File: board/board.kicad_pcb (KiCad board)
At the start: 2 copper layers, 45 x 29 mm, 32 parts, among them J1 019_100BASE-T_with_CT, J2 LPJ4265BDNL, U2 MP8007, U3 POE30P-50L

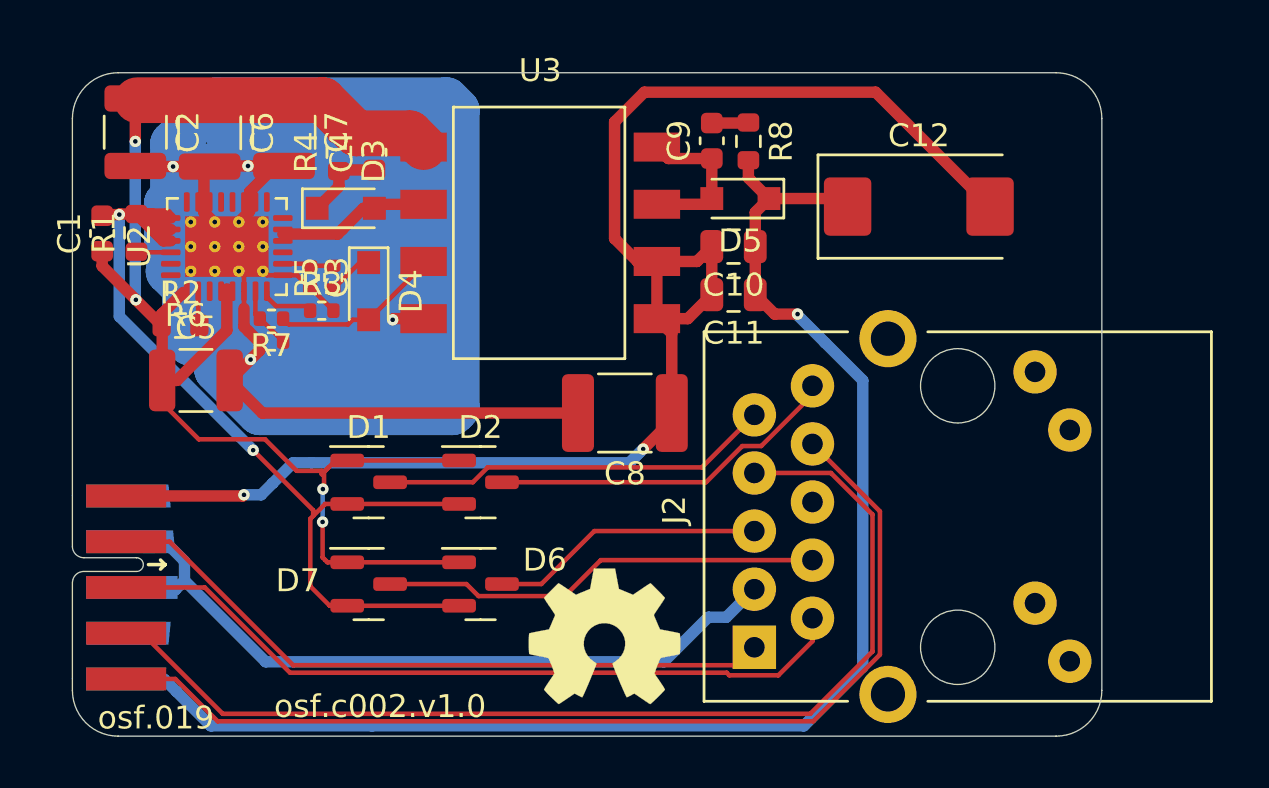
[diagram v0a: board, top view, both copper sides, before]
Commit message: cleaned up silkscreen
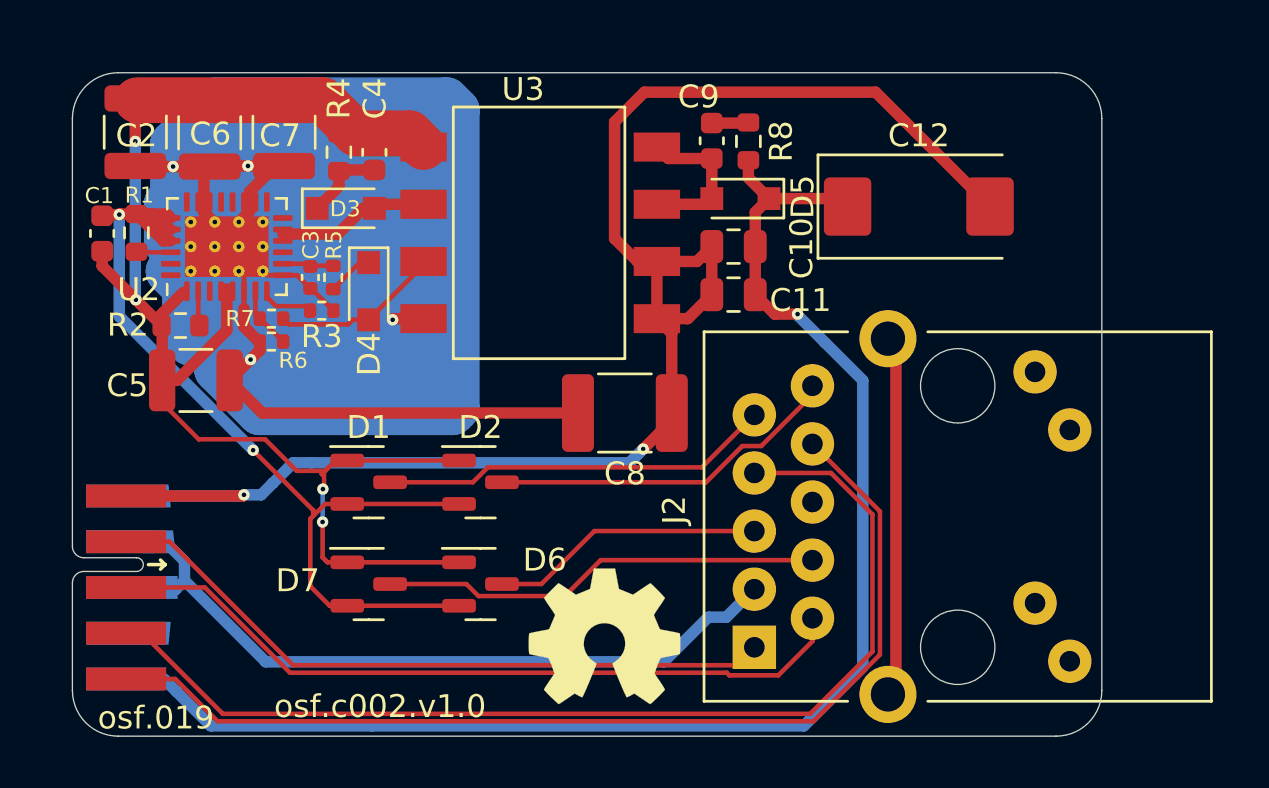
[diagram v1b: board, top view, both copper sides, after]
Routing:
- net /magjack/SH: track 0.00 -> 15.8 mm
- net GND: track 66.4 -> 71.5 mm
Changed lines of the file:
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@@
     (property "Voltage" "100V")
     (attr smd)
-    (fp_text reference "C2" (at 0 -2.3 90) (layer "F.SilkS")
+    (fp_text reference "C2" (at 0.15 -0.05 180) (layer "F.SilkS")
       (effects (font (size 1 1) (thickness 0.15)))
     )
@@
     (property "Sheetname" "Controller")
     (attr smd)
-    (fp_text reference "D5" (at 0 -1.85) (layer "F.SilkS")
+    (fp_text reference "D5" (at -2.725 0.075 90) (layer "F.SilkS")
       (effects (font (size 1 1) (thickness 0.15)))
     )
@@
     (property "Voltage" "100V")
     (attr smd)
-    (fp_text reference "C4" (at 0 -1.43 90) (layer "F.SilkS")
+    (fp_text reference "C4" (at 2.35 0.025 90) (layer "F.SilkS")
       (effects (font (size 1 1) (thickness 0.15)))
     )
@@
     (property "Sheetname" "Controller")
     (attr smd)
-    (fp_text reference "R1" (at 0 -1.43 90) (layer "F.SilkS")
-      (effects (font (size 1 1) (thickness 0.15)))
+    (fp_text reference "R1" (at 1.65 0.125 180) (layer "F.SilkS")
+      (effects (font (size 0.7 0.7) (thickness 0.15)))
     )
     (fp_text value "41.2R" (at 0 1.43 90) (layer "F.Fab")
@@
     (property "Sheetname" "Controller")
     (attr smd)
-    (fp_text reference "D4" (at 0 -1.85 90) (layer "F.SilkS")
+    (fp_text reference "D4" (at 2.75 -0.025 90) (layer "F.SilkS")
       (effects (font (size 1 1) (thickness 0.15)))
     )
@@
     (property "Sheetname" "Controller")
     (attr smd)
-    (fp_text reference "D3" (at 1.22 -2.07 90) (layer "F.SilkS")
-      (effects (font (size 1 1) (thickness 0.15)))
+    (fp_text reference "D3" (at -0.025 0.025 180) (layer "F.SilkS")
+      (effects (font (size 0.7 0.7) (thickness 0.15)))
     )
     (fp_text value "BAV21WS-HE3-18" (at 0.1 1.9) (layer "F.Fab")
@@
     (property "Sheetname" "Controller")
     (attr smd)
-    (fp_text reference "C3" (at 0 -1.16 90) (layer "F.SilkS")
-      (effects (font (size 1 1) (thickness 0.15)))
+    (fp_text reference "C3" (at -1.425 -0.025 90) (layer "F.SilkS")
+      (effects (font (size 0.7 0.7) (thickness 0.15)))
     )
     (fp_text value "100nF" (at 0 1.16 90) (layer "F.Fab")
@@
     (property "Voltage" "100V")
     (attr smd)
-    (fp_text reference "C5" (at 0 -2.3) (layer "F.SilkS")
+    (fp_text reference "C5" (at -3 0.225) (layer "F.SilkS")
       (effects (font (size 1 1) (thickness 0.15)))
     )
@@
     (property "Sheetname" "Controller")
     (attr through_hole)
-    (fp_text reference "U3" (at 0 -7.1) (layer "F.SilkS")
+    (fp_text reference "U3" (at -0.75 -6.275) (layer "F.SilkS")
       (effects (font (size 1 1) (thickness 0.15)))
     )
@@
     (property "Sheetname" "Controller")
     (attr smd)
-    (fp_text reference "R7" (at 0 -1.17) (layer "F.SilkS")
-      (effects (font (size 1 1) (thickness 0.15)))
+    (fp_text reference "R7" (at 1.375 0) (layer "F.SilkS")
+      (effects (font (size 0.7 0.7) (thickness 0.15)))
     )
     (fp_text value "100k" (at 0 1.17) (layer "F.Fab")
@@
     (property "Voltage" "100V")
     (attr smd)
-    (fp_text reference "C9" (at 0 -1.43 90) (layer "F.SilkS")
+    (fp_text reference "C9" (at 1.925 -0.575 180) (layer "F.SilkS")
       (effects (font (size 1 1) (thickness 0.15)))
     )
@@
     (property "Voltage" "6.3V")
     (attr smd)
-    (fp_text reference "C11" (at 0 -1.68) (layer "F.SilkS")
+    (fp_text reference "C11" (at -2.925 -0.25) (layer "F.SilkS")
       (effects (font (size 1 1) (thickness 0.15)))
     )
@@
     (property "Voltage" "100V")
     (attr smd)
-    (fp_text reference "C7" (at 0 -2.3 90) (layer "F.SilkS")
+    (fp_text reference "C7" (at 0.15 0.175 180) (layer "F.SilkS")
       (effects (font (size 1 1) (thickness 0.15)))
     )
@@
     (property "Sheetname" "Controller")
     (attr smd)
-    (fp_text reference "R6" (at -3.75 -1.145) (layer "F.SilkS")
-      (effects (font (size 1 1) (thickness 0.15)))
+    (fp_text reference "R6" (at 0.95 0.825) (layer "F.SilkS")
+      (effects (font (size 0.7 0.7) (thickness 0.15)))
     )
     (fp_text value "20k" (at 0 1.17) (layer "F.Fab")
@@
     (property "Sheetname" "Controller")
     (attr smd)
-    (fp_text reference "U2" (at 0 -3.82 90) (layer "F.SilkS")
+    (fp_text reference "U2" (at -1.875 -3.85 180) (layer "F.SilkS")
       (effects (font (size 1 1) (thickness 0.15)))
     )
@@
     (property "Voltage" "6.3V")
     (attr smd)
-    (fp_text reference "C10" (at 0 -1.68) (layer "F.SilkS")
+    (fp_text reference "C10" (at -2.975 -0.075 90) (layer "F.SilkS")
       (effects (font (size 1 1) (thickness 0.15)))
     )
@@
     (property "Sheetname" "Controller")
     (attr smd)
-    (fp_text reference "R2" (at 0 -1.43) (layer "F.SilkS")
+    (fp_text reference "R2" (at -2.3 -0.025) (layer "F.SilkS")
       (effects (font (size 1 1) (thickness 0.15)))
     )
@@
     (property "Voltage" "100V")
     (attr smd)
-    (fp_text reference "C6" (at 0 -2.3 90) (layer "F.SilkS")
+    (fp_text reference "C6" (at 0.05 -0.025 180) (layer "F.SilkS")
       (effects (font (size 1 1) (thickness 0.15)))
     )
@@
     (property "Sheetname" "Controller")
     (attr smd)
-    (fp_text reference "R5" (at 0 -1.17 90) (layer "F.SilkS")
-      (effects (font (size 1 1) (thickness 0.15)))
+    (fp_text reference "R5" (at 1.425 0.025 90) (layer "F.SilkS")
+      (effects (font (size 0.7 0.7) (thickness 0.15)))
     )
     (fp_text value "5k" (at 0 1.17 90) (layer "F.Fab")
@@
     (property "Sheetname" "Controller")
     (attr smd)
-    (fp_text reference "R4" (at 0 -1.43 90) (layer "F.SilkS")
+    (fp_text reference "R4" (at 2.35 0 90) (layer "F.SilkS")
       (effects (font (size 1 1) (thickness 0.15)))
     )
@@
     (property "Sheetname" "Controller")
     (attr smd)
-    (fp_text reference "C1" (at 0 -1.43 90) (layer "F.SilkS")
-      (effects (font (size 1 1) (thickness 0.15)))
+    (fp_text reference "C1" (at 1.65 -0.125 180) (layer "F.SilkS")
+      (effects (font (size 0.7 0.7) (thickness 0.15)))
     )
     (fp_text value "100n" (at 0 1.43 90) (layer "F.Fab")
@@
     (property "Sheetname" "Controller")
     (attr smd)
-    (fp_text reference "R3" (at 0 -1.17) (layer "F.SilkS")
+    (fp_text reference "R3" (at 0 1.125) (layer "F.SilkS")
       (effects (font (size 1 1) (thickness 0.15)))
     )
@@
   (segment (start 155.35 77.25) (end 154.75 76.65) (width 2) (layer "F.Cu") (net 1))
   (segment (start 150.95 75.2) (end 142.825 75.2) (width 2) (layer "F.Cu") (net 1))
-  (segment (start 146.025 75.125) (end 146 75.15) (width 0.5) (layer "F.Cu") (net 1))
   (segment (start 149.8 91.4) (end 150.9 91.4) (width 0.2) (layer "F.Cu") (net 1))
   (segment (start 156.9025 95.4) (end 152.0125 95.4) (width 0.2) (layer "F.Cu") (net 1))
@@
   (segment (start 166.2 88.875) (end 166.2 89.2) (width 0.5) (layer "F.Cu") (net 9))
   (segment (start 166.2 85.4) (end 165.55 84.75) (width 0.5) (layer "F.Cu") (net 9))
-  (segment (start 147.5 92.45) (end 147.45 92.5) (width 0.5) (layer "F.Cu") (net 9))
   (segment (start 167.95 83.7) (end 167.95 81.6) (width 0.5) (layer "F.Cu") (net 9))
   (segment (start 165.55 82.25) (end 167.3 82.25) (width 0.5) (layer "F.Cu") (net 9))
   (segment (start 163.7 76.15) (end 163.7 81.25) (width 0.5) (layer "F.Cu") (net 9))
   (segment (start 165.55 84.75) (end 165.55 82.25) (width 0.5) (layer "F.Cu") (net 9))
-  (segment (start 147.45 92.5) (end 142.35 92.5) (width 0.5) (layer "F.Cu") (net 9))
   (segment (start 166.9 84.75) (end 167.95 83.7) (width 0.5) (layer "F.Cu") (net 9))
   (segment (start 165.55 84.75) (end 166.9 84.75) (width 0.5) (layer "F.Cu") (net 9))
   (segment (start 180.1125 79.85) (end 175.1125 74.85) (width 0.5) (layer "F.Cu") (net 9))
+  (segment (start 142.35 92.5) (end 147.45 92.5) (width 0.5) (layer "F.Cu") (net 9))
   (segment (start 166.2 88.875) (end 166.2 85.4) (width 0.5) (layer "F.Cu") (net 9))
   (segment (start 163.7 81.25) (end 164.7 82.25) (width 0.5) (layer "F.Cu") (net 9))
@@
   (segment (start 166.2 89.2) (end 164.95 90.45) (width 0.5) (layer "F.Cu") (net 9))
   (segment (start 167.3 82.25) (end 167.95 81.6) (width 0.5) (layer "F.Cu") (net 9))
+  (segment (start 147.45 92.5) (end 147.5 92.45) (width 0.5) (layer "F.Cu") (net 9))
   (via (at 147.5 92.45) (size 0.5) (drill 0.2) (layers "F.Cu" "B.Cu") (net 9))
   (via (at 164.95 90.45) (size 0.5) (drill 0.2) (layers "F.Cu" "B.Cu") (net 9))
   (segment (start 164.35 91.05) (end 150.45 91.05) (width 0.5) (layer "B.Cu") (net 9))
+  (segment (start 142.4 92.5) (end 147.45 92.5) (width 0.5) (layer "B.Cu") (net 9))
   (segment (start 150.45 91.05) (end 149.65 91.05) (width 0.5) (layer "B.Cu") (net 9))
   (segment (start 148.75 91.95) (end 148.25 92.45) (width 0.5) (layer "B.Cu") (net 9))
   (segment (start 148.25 92.45) (end 147.5 92.45) (width 0.5) (layer "B.Cu") (net 9))
+  (segment (start 147.45 92.5) (end 147.5 92.45) (width 0.5) (layer "B.Cu") (net 9))
   (segment (start 164.95 90.45) (end 164.35 91.05) (width 0.5) (layer "B.Cu") (net 9))
   (segment (start 149.65 91.05) (end 148.75 91.95) (width 0.5) (layer "B.Cu") (net 9))
@@
   (segment (start 142.7 96.6) (end 142.6 96.5) (width 0.5) (layer "B.Cu") (net 25))
   (segment (start 167.8 97.8) (end 168.585 97.8) (width 0.5) (layer "B.Cu") (net 25))
+  (segment (start 175.65 85.625) (end 176 85.975) (width 0.5) (layer "F.Cu") (net 30))
+  (segment (start 176 85.975) (end 176 100.825) (width 0.5) (layer "F.Cu") (net 30))
+  (segment (start 176 100.825) (end 175.65 101.175) (width 0.5) (layer "F.Cu") (net 30))
 )

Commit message: added LDO
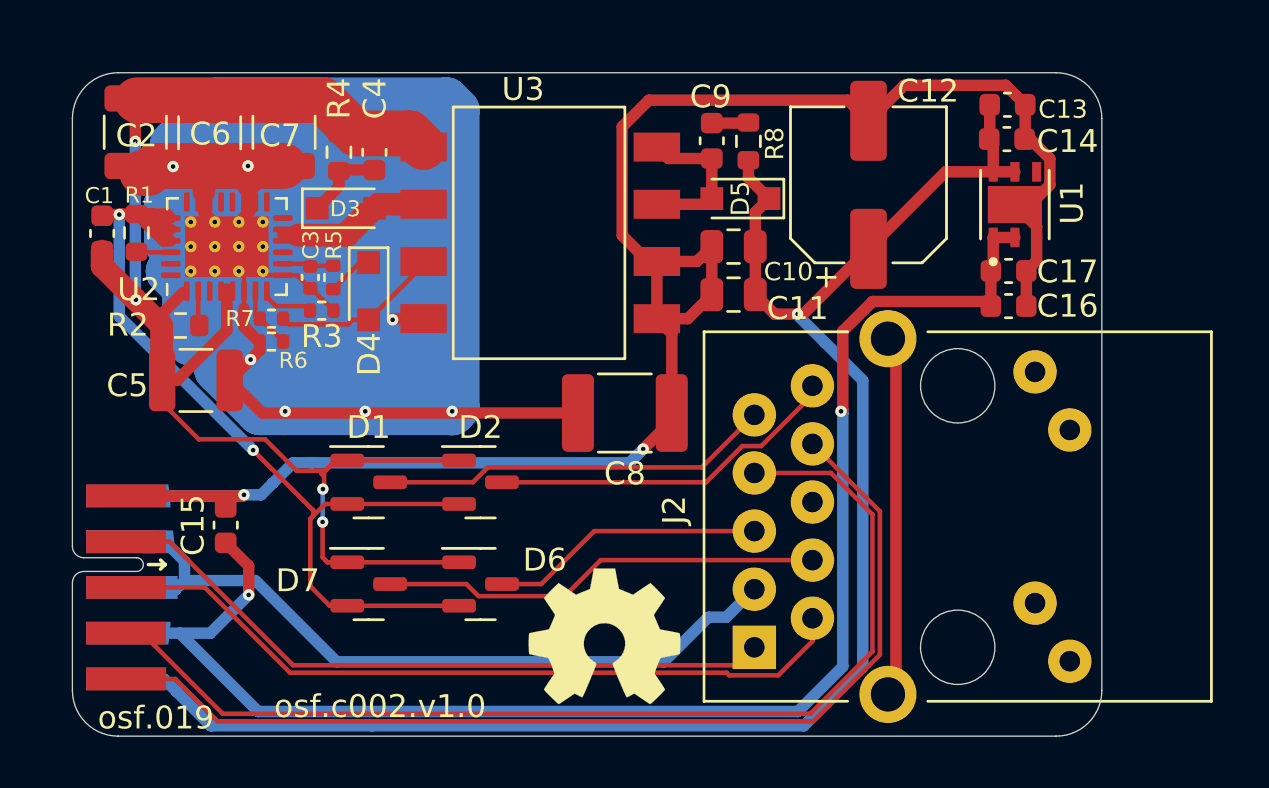
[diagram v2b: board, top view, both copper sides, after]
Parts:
- added C13: 1uF, Capacitor_SMD:C_0603_1608Metric, F.Cu at (180.9, 75.4)
- added C14: 10uF, Capacitor_SMD:C_0603_1608Metric, F.Cu at (180.8, 76.9)
- added C15: 10uF, Capacitor_SMD:C_0603_1608Metric, F.Cu at (146.7, 93.8)
- added C16: 10uF, Capacitor_SMD:C_0603_1608Metric, F.Cu at (180.9, 84.2)
- added C17: 1uF, Capacitor_SMD:C_0603_1608Metric, F.Cu at (180.9, 82.7)
- added U1: LD39200PU33R, b121:SON95P300X300X100-7N, F.Cu at (181.2, 79.8)
- C12: value 220u -> 220uF; footprint Capacitor_Tantalum_SMD:CP_EIA-7343-31_Kemet-D -> Capacitor_SMD:CP_Elec_6.3x5.9
- moved C12 2.40 mm to (174.8, 78.9), turned to 90 degrees
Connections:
- J1 pad 9: unconnected-(J1-Pad9) -> /ldo/3.3v
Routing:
- net /ldo/3.3v: track 0.00 -> 65.7 mm, vias 0 -> 2
- net /Controller/5V: track 63.1 -> 74.6 mm
- net GND: track 71.5 -> 82.4 mm
- net /Controller/GNDPWR: track 196.7 -> 204.1 mm, vias 4 -> 7
- net Net-(D3-A): track 6.69 -> 10.5 mm
- net /Controller/PoE+: track 63.0 -> 66.7 mm

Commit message: tuned ILIM resistor and voltage divider of flyback
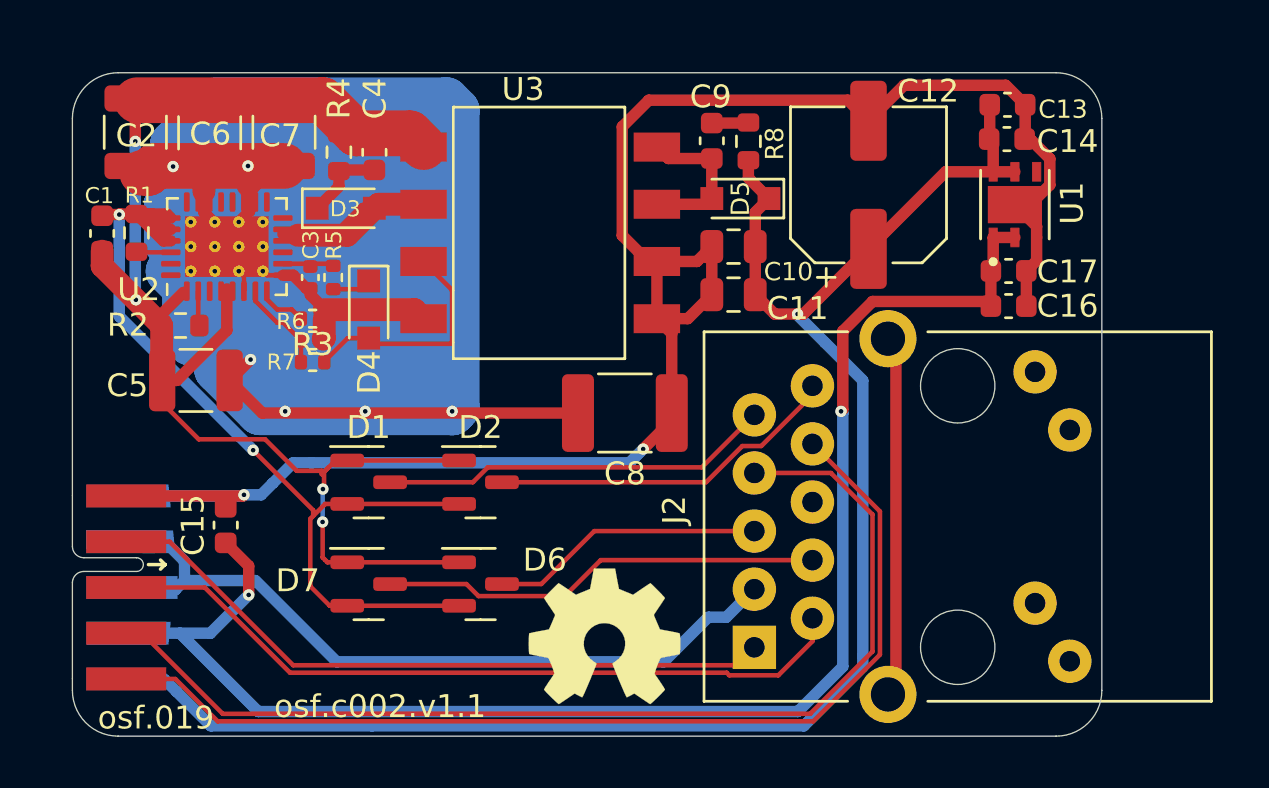
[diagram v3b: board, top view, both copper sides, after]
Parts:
- moved R7 2.62 mm to (150.5, 86.7)
- moved R6 1.80 mm to (150.5, 85.7), turned to 180 degrees
- moved D4 0.80 mm to (152.9, 84.3)
- moved R3 0.53 mm to (150.5, 84.8)
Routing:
- net Net-(D4-A): track 7.47 -> 10.2 mm
- net /Controller/GNDPWR: track 204.1 -> 205.8 mm, vias 7 -> 6
- net Net-(U2-FB1): track 2.71 -> 4.08 mm
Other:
- board text added: "osf.c002.v1.1"
- board text removed: "osf.c002.v1.0"

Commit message: made bulk cap footprint larger
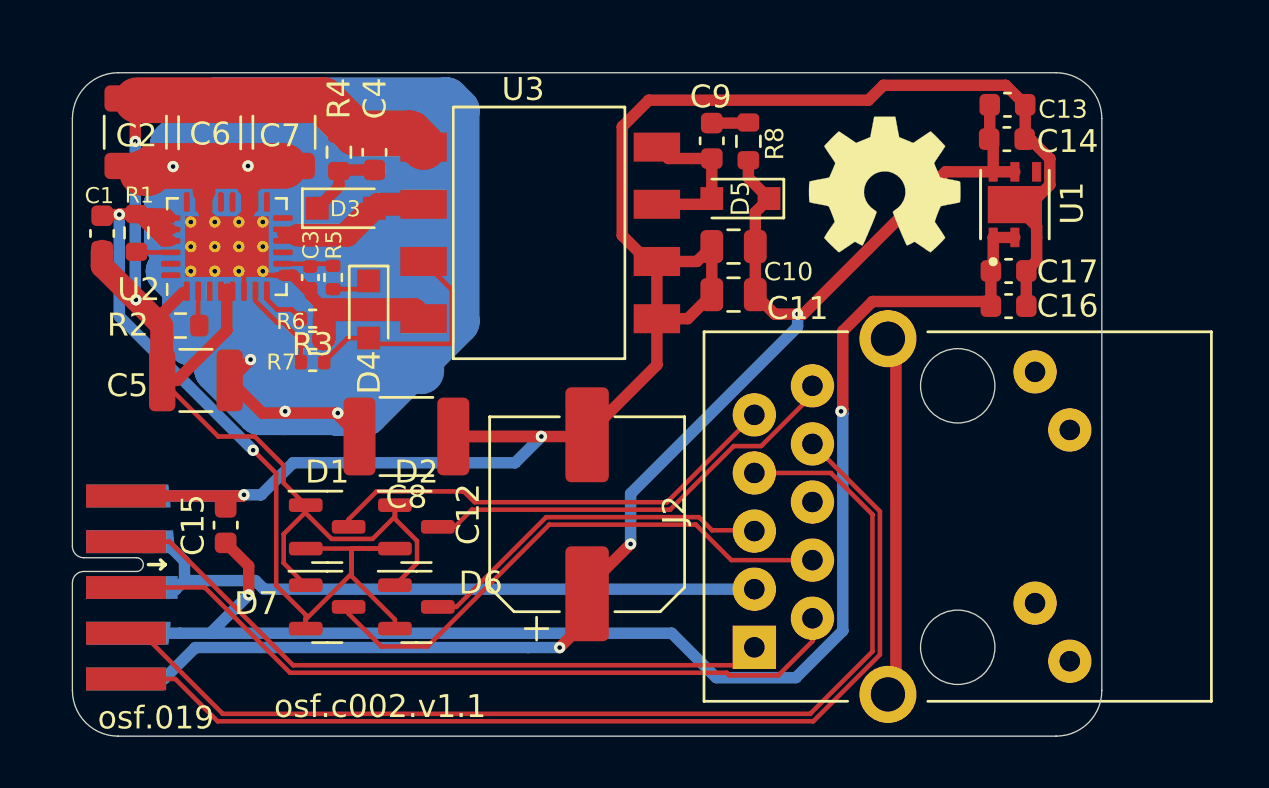
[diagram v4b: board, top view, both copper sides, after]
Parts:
- C12: footprint Capacitor_SMD:CP_Elec_6.3x5.9 -> Capacitor_SMD:CP_Elec_8x6.9
- R3: value 100k -> 316k
- R7: value 100k -> 121k
- moved LOGO1 23.2 mm to (175.5, 78.9)
- moved C12 18.9 mm to (162.5, 93.3)
- moved C8 9.60 mm to (154.6, 89.9)
- moved D2 3.41 mm to (155.0, 93.8)
- moved D6 2.98 mm to (155.0, 97.3)
- moved D1 2.66 mm to (151.1, 93.8)
- moved D7 2.07 mm to (151.1, 97.3)
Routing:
- net /Controller/5V: track 74.6 -> 62.2 mm, vias 1 -> 3
- net /Controller/GNDPWR: track 205.8 -> 194.3 mm, vias 6 -> 5
- net /magjack/CT4: track 19.3 -> 24.0 mm
- net GND: track 82.4 -> 87.0 mm
- net /magjack/CT3: track 12.0 -> 15.7 mm
- net /magjack/CT2: track 15.5 -> 19.2 mm
- net /ldo/3.3v: track 65.7 -> 62.2 mm
- net /magjack/CT1: track 17.1 -> 20.3 mm
- net /magjack/CT: track 34.2 -> 31.6 mm
- net /Controller/PoE-: track 40.1 -> 42.8 mm
- net /Controller/PoE+: track 66.7 -> 64.2 mm, vias 4 -> 2
